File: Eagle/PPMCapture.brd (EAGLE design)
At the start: 30.5 x 16.2 mm, 4 parts, among them U1 ATTINY85V-10P

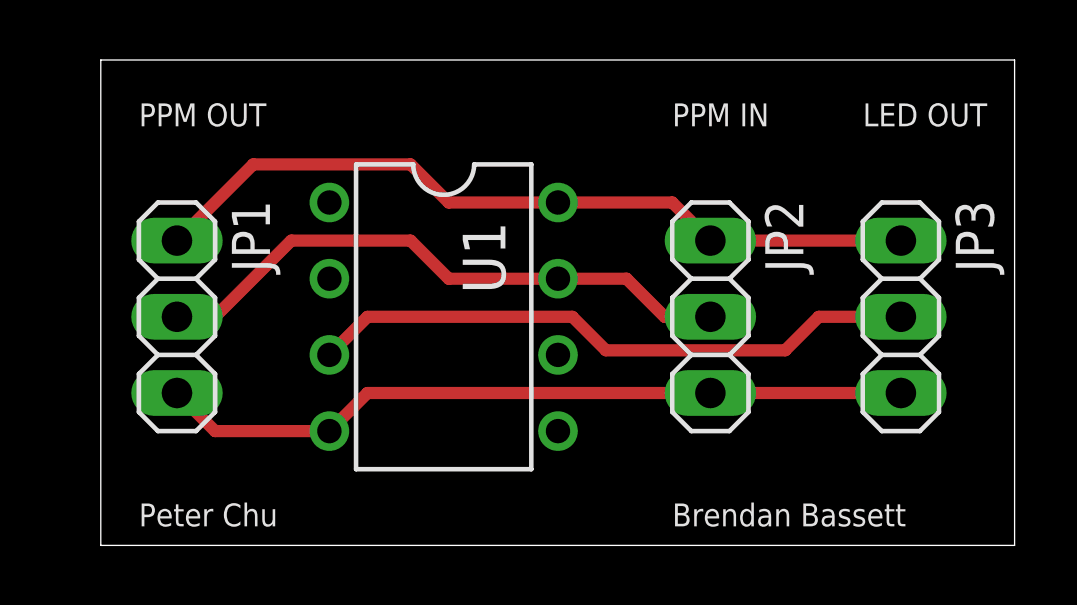
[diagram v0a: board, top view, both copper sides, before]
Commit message: Chaned .1 header to JST 3pin connector
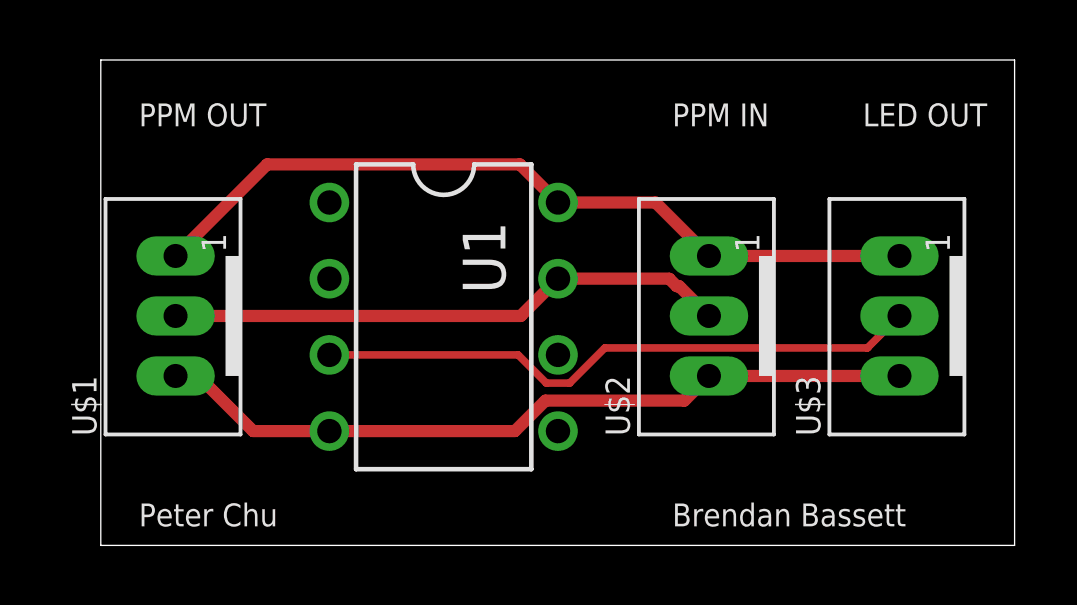
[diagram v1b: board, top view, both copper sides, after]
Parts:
- removed JP1, JP2, JP3: (no value), GTOR - Connectors:1X03
- added U$1, U$2, U$3: JST-PH_3-PIN_HEADER, SRG:JST_B3B-PH_HEADER
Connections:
- net +5V: now also U$1.P1, U$2.P1, U$3.P1; no longer JP1.1, JP2.1, JP3.1
- net GND: now also U$1.P3, U$2.P3, U$3.P3; no longer JP1.3, JP2.3, JP3.3
- net LEDOUT: now also U$3.P2; no longer JP3.2
- net PPM: now also U$1.P2, U$2.P2; no longer JP1.2, JP2.2
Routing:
- net PPM: track 19.9 -> 18.8 mm

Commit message: Flipped board for PCB milling
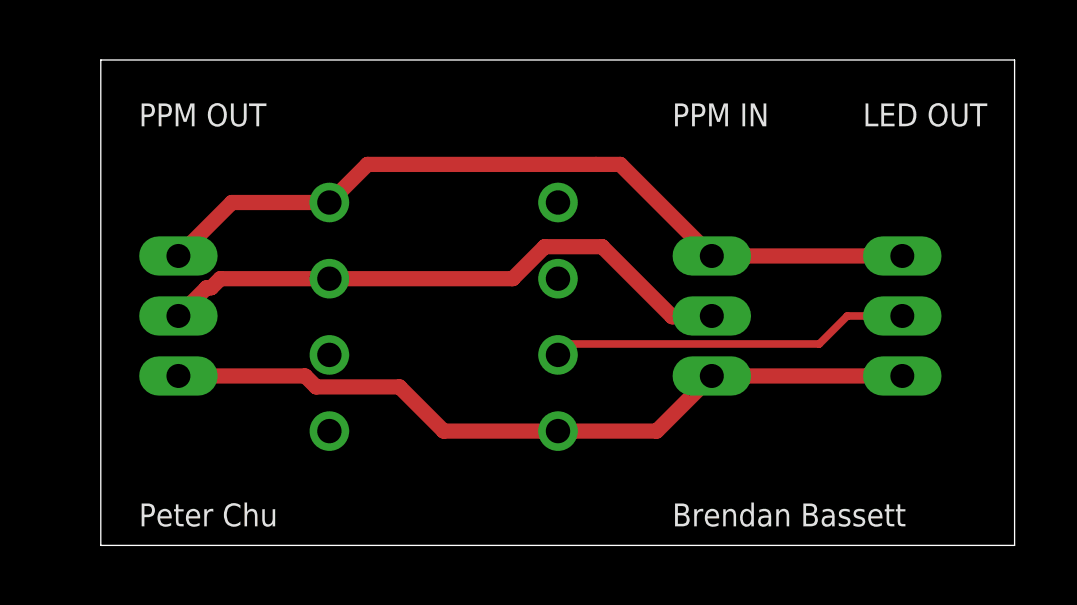
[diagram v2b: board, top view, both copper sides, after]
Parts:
- flipped U$1 to the bottom
- flipped U$2 to the bottom
- flipped U$3 to the bottom
- flipped U1 to the bottom
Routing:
- net LEDOUT: track 20.3 -> 12.0 mm
- net PPM: track 18.8 -> 19.7 mm
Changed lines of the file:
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@@
 </autorouter>
 <elements>
-<element name="U1" library="_hhn_attiny25_45_85" package="PDIP08_300MIL" value="ATTINY85V-10P" x="11.43" y="7.62" smashed="yes" rot="R270">
-<attribute name="NAME" x="12.065" y="10.795" size="1.4224" layer="25" ratio="9" rot="R270"/>
+<element name="U1" library="_hhn_attiny25_45_85" package="PDIP08_300MIL" value="ATTINY85V-10P" x="11.43" y="7.62" smashed="yes" rot="MR270">
+<attribute name="NAME" x="10.795" y="10.795" size="1.4224" layer="26" ratio="9" rot="MR270"/>
 </element>
-<element name="U$1" library="SRG" package="JST_B3B-PH_HEADER" value="JST-PH_3-PIN_HEADER" x="2.54" y="7.62" smashed="yes" rot="R90">
-<attribute name="NAME" x="-0.1425" y="3.6475" size="0.8128" layer="25" font="vector" rot="R90"/>
+<element name="U$1" library="SRG" package="JST_B3B-PH_HEADER" value="JST-PH_3-PIN_HEADER" x="2.54" y="7.62" smashed="yes" rot="MR90">
+<attribute name="NAME" x="5.2225" y="3.6475" size="0.8128" layer="26" font="vector" rot="MR90"/>
 </element>
-<element name="U$2" library="SRG" package="JST_B3B-PH_HEADER" value="JST-PH_3-PIN_HEADER" x="20.32" y="7.62" smashed="yes" rot="R90">
-<attribute name="NAME" x="17.6375" y="3.6475" size="0.8128" layer="25" font="vector" rot="R90"/>
+<element name="U$2" library="SRG" package="JST_B3B-PH_HEADER" value="JST-PH_3-PIN_HEADER" x="20.32" y="7.62" smashed="yes" rot="MR90">
+<attribute name="NAME" x="23.0025" y="3.6475" size="0.8128" layer="26" font="vector" rot="MR90"/>
 </element>
-<element name="U$3" library="SRG" package="JST_B3B-PH_HEADER" value="JST-PH_3-PIN_HEADER" x="26.67" y="7.62" smashed="yes" rot="R90">
-<attribute name="NAME" x="23.9875" y="3.6475" size="0.8128" layer="25" font="vector" rot="R90"/>
+<element name="U$3" library="SRG" package="JST_B3B-PH_HEADER" value="JST-PH_3-PIN_HEADER" x="26.67" y="7.62" smashed="yes" rot="MR90">
+<attribute name="NAME" x="29.3525" y="3.6475" size="0.8128" layer="26" font="vector" rot="MR90"/>
 </element>
 </elements>
@@
 <contactref element="U$2" pad="P1"/>
 <contactref element="U$1" pad="P1"/>
-<wire x1="2.4925" y1="9.6475" x2="5.545" y2="12.7" width="0.4064" layer="1"/>
-<wire x1="5.545" y1="12.7" x2="13.97" y2="12.7" width="0.4064" layer="1"/>
-<wire x1="13.97" y1="12.7" x2="15.24" y2="11.43" width="0.4064" layer="1"/>
-<wire x1="15.24" y1="11.43" x2="18.49" y2="11.43" width="0.4064" layer="1"/>
-<wire x1="18.49" y1="11.43" x2="20.2725" y2="9.6475" width="0.4064" layer="1"/>
-<wire x1="20.2725" y1="9.6475" x2="26.6225" y2="9.6475" width="0.4064" layer="1"/>
+<wire x1="2.5875" y1="9.6475" x2="4.37" y2="11.43" width="0.508" layer="1"/>
+<wire x1="4.37" y1="11.43" x2="7.62" y2="11.43" width="0.508" layer="1"/>
+<wire x1="7.62" y1="11.43" x2="8.89" y2="12.7" width="0.508" layer="1"/>
+<wire x1="8.89" y1="12.7" x2="16.51" y2="12.7" width="0.508" layer="1"/>
+<wire x1="26.7175" y1="9.6475" x2="20.3675" y2="9.6475" width="0.508" layer="1"/>
+<wire x1="20.3675" y1="9.6475" x2="17.315" y2="12.7" width="0.508" layer="1"/>
+<wire x1="17.315" y1="12.7" x2="16.51" y2="12.7" width="0.508" layer="1"/>
 </signal>
 <signal name="GND">
@@
 <contactref element="U$2" pad="P3"/>
 <contactref element="U$1" pad="P3"/>
-<wire x1="2.4925" y1="5.6475" x2="3.2425" y2="5.6475" width="0.4064" layer="1"/>
-<wire x1="3.2425" y1="5.6475" x2="5.08" y2="3.81" width="0.4064" layer="1"/>
-<wire x1="5.08" y1="3.81" x2="7.62" y2="3.81" width="0.4064" layer="1"/>
-<wire x1="7.62" y1="3.81" x2="13.80315625" y2="3.81" width="0.4064" layer="1"/>
-<wire x1="13.80315625" y1="3.81" x2="14.81915625" y2="4.826" width="0.4064" layer="1"/>
-<wire x1="19.451" y1="4.826" x2="20.2725" y2="5.6475" width="0.4064" layer="1"/>
-<wire x1="14.81915625" y1="4.826" x2="19.451" y2="4.826" width="0.4064" layer="1"/>
-<wire x1="20.2725" y1="5.6475" x2="26.6225" y2="5.6475" width="0.4064" layer="1"/>
+<wire x1="2.5875" y1="5.6475" x2="6.8138125" y2="5.6475" width="0.508" layer="1"/>
+<wire x1="6.8138125" y1="5.6475" x2="7.1781125" y2="5.2832" width="0.508" layer="1"/>
+<wire x1="9.9568" y1="5.2832" x2="11.43" y2="3.81" width="0.508" layer="1"/>
+<wire x1="7.1781125" y1="5.2832" x2="9.9568" y2="5.2832" width="0.508" layer="1"/>
+<wire x1="11.43" y1="3.81" x2="15.24" y2="3.81" width="0.508" layer="1"/>
+<wire x1="15.24" y1="3.81" x2="18.53" y2="3.81" width="0.508" layer="1"/>
+<wire x1="18.53" y1="3.81" x2="20.3675" y2="5.6475" width="0.508" layer="1"/>
+<wire x1="26.7175" y1="5.6475" x2="20.3675" y2="5.6475" width="0.508" layer="1"/>
 </signal>
 <signal name="PPM">
@@
 <contactref element="U$2" pad="P2"/>
 <contactref element="U$1" pad="P2"/>
-<wire x1="2.4925" y1="7.6475" x2="13.9975" y2="7.6475" width="0.4064" layer="1"/>
-<wire x1="13.9975" y1="7.6475" x2="15.24" y2="8.89" width="0.4064" layer="1"/>
-<wire x1="15.24" y1="8.89" x2="18.94820625" y2="8.89" width="0.4064" layer="1"/>
-<wire x1="18.94820625" y1="8.89" x2="19.20030625" y2="8.6379" width="0.4064" layer="1"/>
-<wire x1="19.20030625" y1="8.6379" x2="19.2821" y2="8.6379" width="0.4064" layer="1"/>
-<wire x1="20.2725" y1="7.6475" x2="19.2821" y2="8.6379" width="0.4064" layer="1"/>
+<wire x1="2.5875" y1="7.6475" x2="3.5271" y2="8.5871" width="0.508" layer="1"/>
+<wire x1="3.5271" y1="8.5871" x2="3.6807375" y2="8.5871" width="0.508" layer="1"/>
+<wire x1="3.6807375" y1="8.5871" x2="3.9836375" y2="8.89" width="0.508" layer="1"/>
+<wire x1="3.9836375" y1="8.89" x2="7.62" y2="8.89" width="0.508" layer="1"/>
+<wire x1="7.62" y1="8.89" x2="13.7313125" y2="8.89" width="0.508" layer="1"/>
+<wire x1="13.7313125" y1="8.89" x2="14.7981125" y2="9.9568" width="0.508" layer="1"/>
+<wire x1="14.7981125" y1="9.9568" x2="16.7132" y2="9.9568" width="0.508" layer="1"/>
+<wire x1="16.7132" y1="9.9568" x2="19.05" y2="7.62" width="0.508" layer="1"/>
+<wire x1="19.05" y1="7.62" x2="20.34" y2="7.62" width="0.508" layer="1"/>
+<wire x1="20.34" y1="7.62" x2="20.3675" y2="7.6475" width="0.508" layer="1"/>
 </signal>
 <signal name="LEDOUT">
 <contactref element="U1" pad="3"/>
 <contactref element="U$3" pad="P2"/>
-<wire x1="15.62928125" y1="5.4102" x2="14.85071875" y2="5.4102" width="0.254" layer="1"/>
-<wire x1="13.91091875" y1="6.35" x2="7.62" y2="6.35" width="0.254" layer="1"/>
-<wire x1="14.85071875" y1="5.4102" x2="13.91091875" y2="6.35" width="0.254" layer="1"/>
-<wire x1="26.6225" y1="7.6475" x2="25.5559" y2="6.5809" width="0.254" layer="1"/>
-<wire x1="25.5559" y1="6.5809" x2="16.79998125" y2="6.5809" width="0.254" layer="1"/>
-<wire x1="16.79998125" y1="6.5809" x2="15.62928125" y2="5.4102" width="0.254" layer="1"/>
+<wire x1="24.88153125" y1="7.6475" x2="26.7175" y2="7.6475" width="0.254" layer="1"/>
+<wire x1="23.94813125" y1="6.7141" x2="24.88153125" y2="7.6475" width="0.254" layer="1"/>
+<wire x1="15.24" y1="6.35" x2="15.6041" y2="6.7141" width="0.254" layer="1"/>
+<wire x1="15.6041" y1="6.7141" x2="23.94813125" y2="6.7141" width="0.254" layer="1"/>
 </signal>
 </signals>
